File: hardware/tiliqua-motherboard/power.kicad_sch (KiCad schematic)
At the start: 23 parts, among them J6 CONN 2x5 P=2.54mm, U5 AP63200WU

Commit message: R2 start
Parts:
- removed C35: 100nF, Capacitor_SMD:C_0603_1608Metric, symbol Device:C_Small
- removed C36: 22.0uF, Capacitor_Tantalum_SMD:CP_EIA-3216-10_Kemet-I, symbol Device:C_Polarized_Small
- removed D6: 1N4007FL, Diode_SMD:D_SOD-123F, symbol Diode:US1G
- added C27, C29, C39: 47uF, Capacitor_SMD:CP_Elec_6.3x5.4, symbol Device:C_Polarized_Small
- added C28: 100nF, Capacitor_SMD:C_0603_1608Metric, symbol Device:C_Small
- added C38: 22uF, Capacitor_Tantalum_SMD:CP_EIA-3216-10_Kemet-I, symbol Device:C_Polarized_Small
- added L4, L5, L6, L7: FERRITE, Inductor_SMD:L_0603_1608Metric, symbol Device:L_Ferrite_Small
- added U6: AMS1117-3.3, Package_TO_SOT_SMD:SOT-223-3_TabPin2, symbol Regulator_Linear:AMS1117-3.3
- C32: value 22.0uF -> 22uF
- C33: value 22.0uF -> 47uF; footprint Capacitor_Tantalum_SMD:CP_EIA-3216-10_Kemet-I -> Capacitor_SMD:CP_Elec_6.3x5.4; lcsc# C782264 -> C88735; mfg# CA45-A-16V-22uF-K -> 25SEV47M6.3X5.5
- L3: value 6.8uH 2A -> 10uH 2A; lcsc# C844992 -> (none)
- R17: value 182K -> 157K; PN RC0402FR-074K7L -> (none); lcsc# C327365 -> (none)
- R18: value 62K -> 30K; PN RC0402FR-074K7L -> (none); lcsc# C137950 -> (none)
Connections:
- net VAUX is gone; now on net +12V: U5.2 (EN), U5.3 (IN)
- net +12V: now also C27.1, L6.2
- net +3V3: now also U6.2 (VO); no longer C31.2, C34.1, L3.2, R17.2
- net -12V: now also L7.2
- net GND: now also C27.2, C28.2, C29.2, C38.2, C39.2, U6.1 (GND)
- net at D3.2 (A), L2.2: now also L7.1
- net at D2.1 (K), L1.2: now also L6.1
- new net: C28.1, C29.1, L4.1, L5.1, U6.3 (VI)
- new net +5V: C31.2, C34.1, C38.1, C39.1, L3.2, L4.2, L5.2, R17.2
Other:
- moved on the sheet: C22, C23, C24, C25, C34

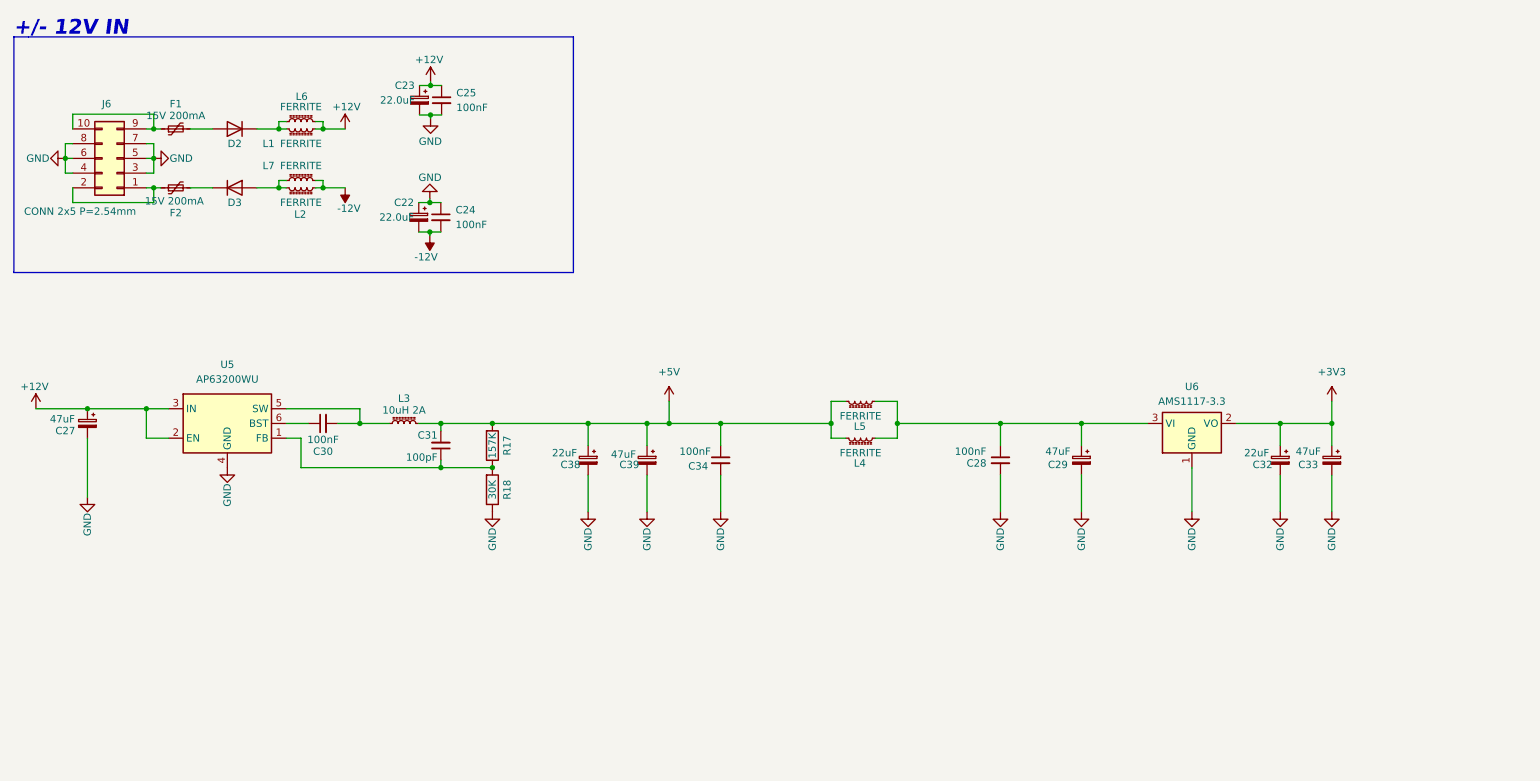
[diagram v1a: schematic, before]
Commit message: schematic cleanup, dual-role usb c
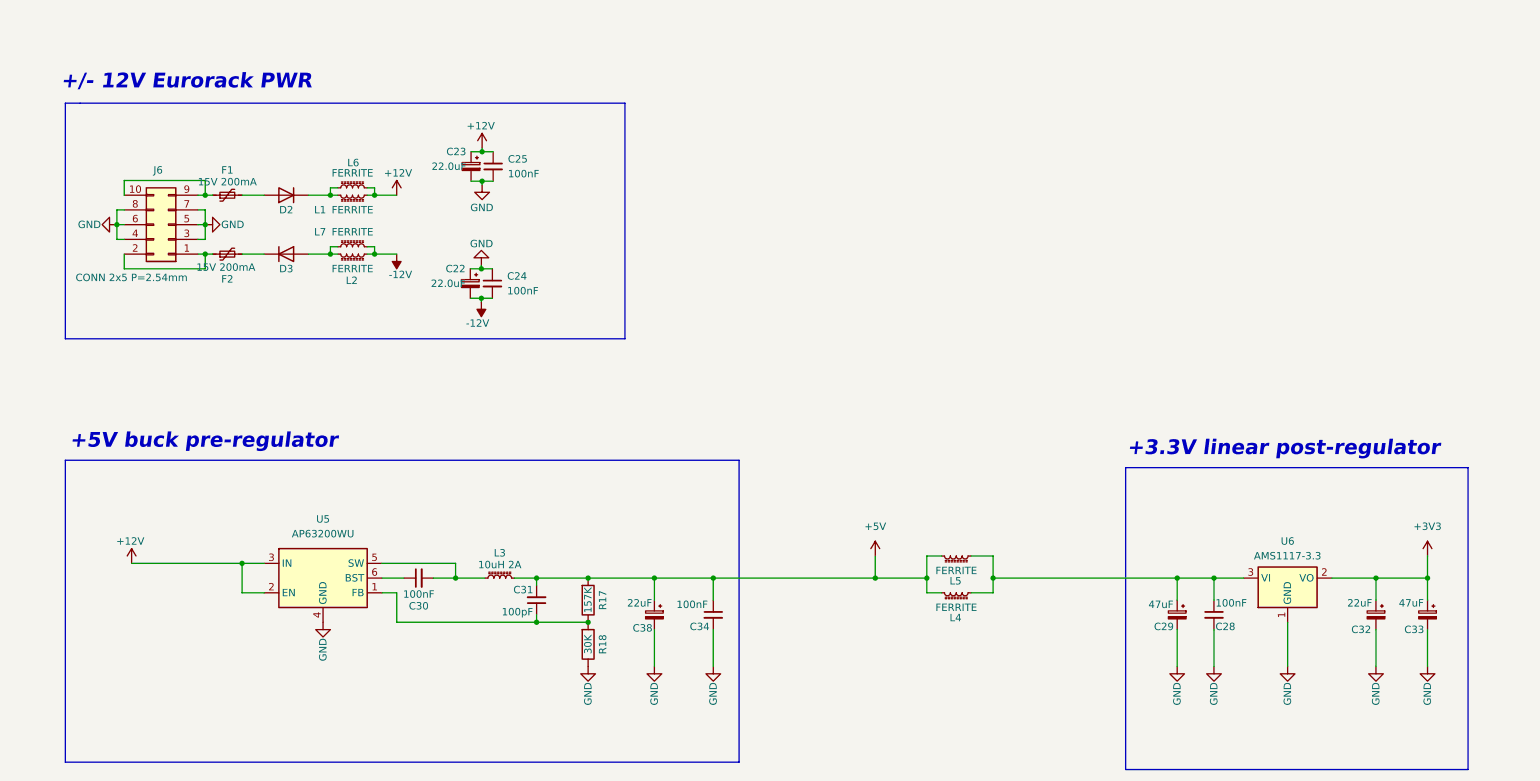
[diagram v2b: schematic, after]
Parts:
- removed C27, C39: 47uF, Capacitor_SMD:CP_Elec_6.3x5.4, symbol Device:C_Polarized_Small
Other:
- note added: "+/- 12V Eurorack PWR"
- note added: "+3.3V linear post-regulator"
- note added: "+5V buck pre-regulator"
- note removed: "+/- 12V IN"
- moved on the sheet: C22, C23, C24, C25, C28, C29, C30, C31, C32, C33, C34, C38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

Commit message: place most parts
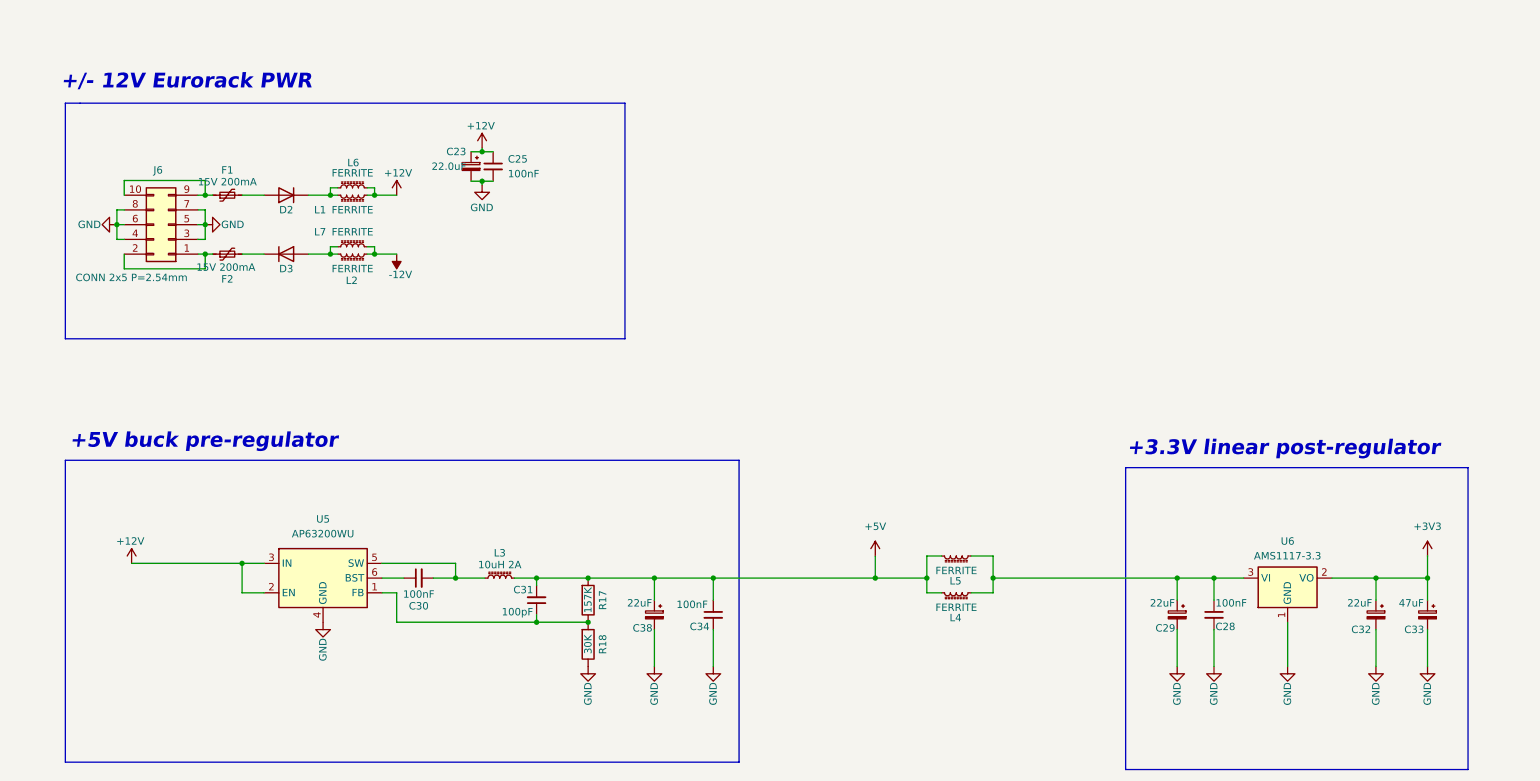
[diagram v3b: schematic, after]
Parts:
- removed C22: 22.0uF, Capacitor_Tantalum_SMD:CP_EIA-3216-10_Kemet-I, symbol Device:C_Polarized_Small
- removed C24: 100nF, Capacitor_SMD:C_0603_1608Metric, symbol Device:C_Small
- C29: value 47uF -> 22uF; footprint Capacitor_SMD:CP_Elec_6.3x5.4 -> Capacitor_Tantalum_SMD:CP_EIA-3216-10_Kemet-I; lcsc# C88735 -> C782264; mfg# 25SEV47M6.3X5.5 -> CA45-A-16V-22uF-K

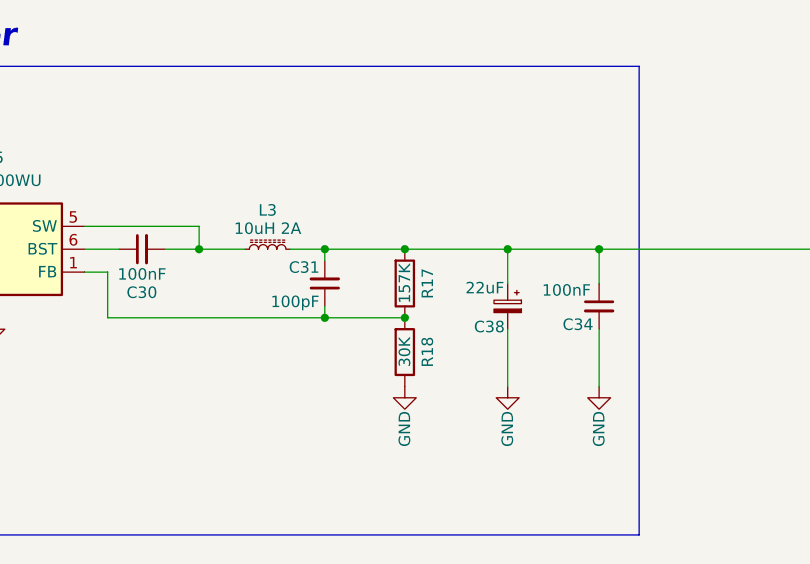
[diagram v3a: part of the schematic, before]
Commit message: add some part numbers
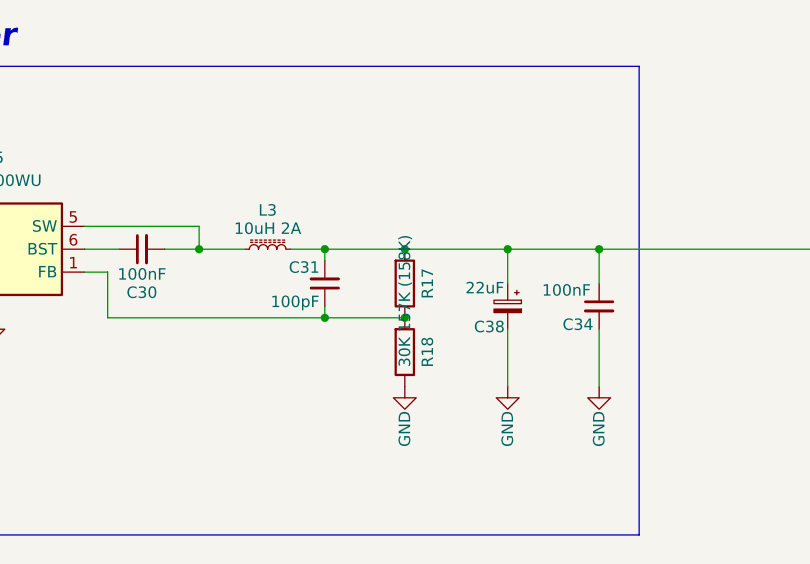
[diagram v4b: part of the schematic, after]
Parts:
- L3: lcsc# (none) -> C844996
- R17: value 157K -> 157K (158K); lcsc# (none) -> C861679
- R18: lcsc# (none) -> C25776
- U6: lcsc# (none) -> C347222

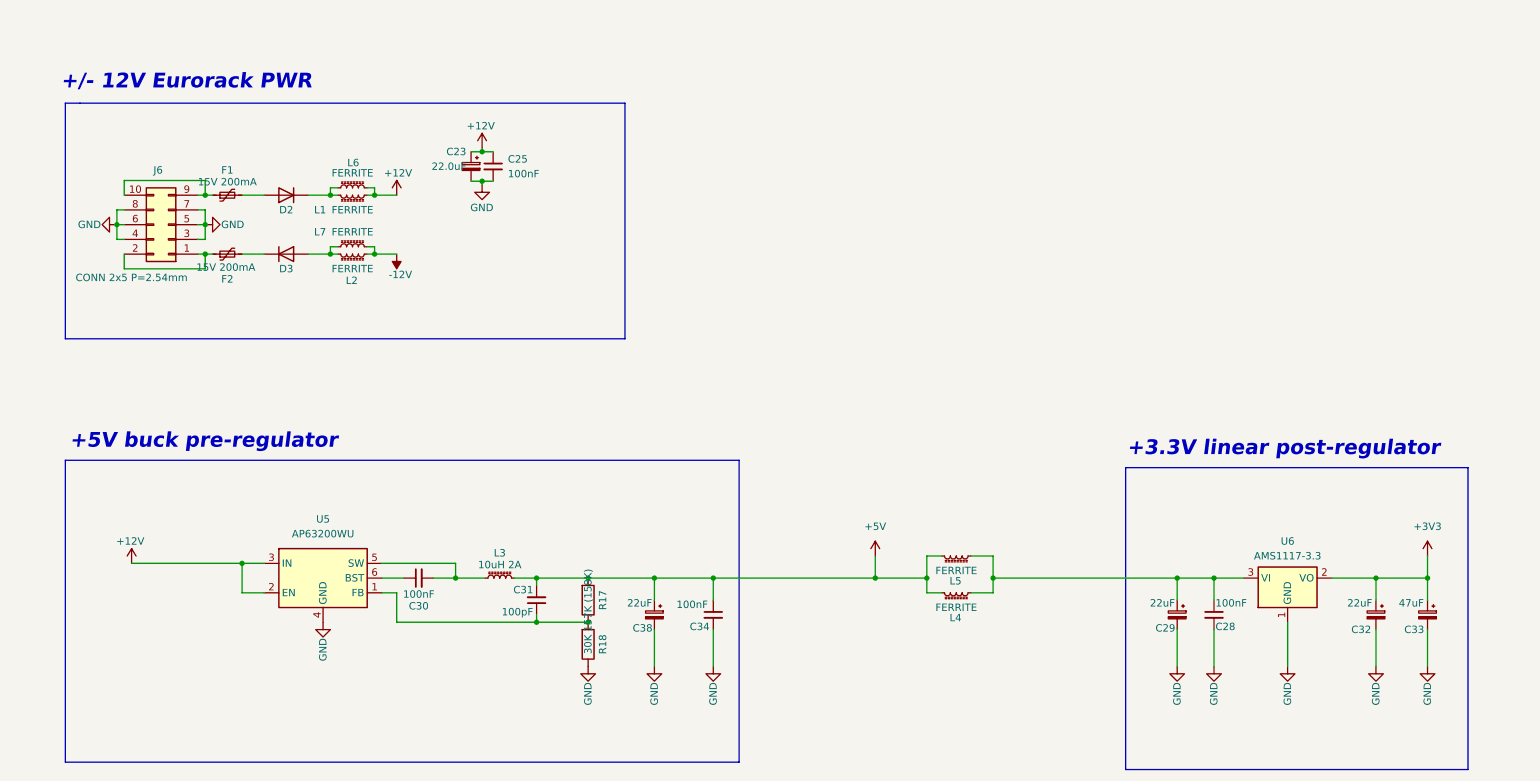
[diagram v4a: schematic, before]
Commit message: hw/mobo-r3: swap tantalums for ceramics, clean up PSU routing, swap LDO for TPS7A91, add choke input capacitors
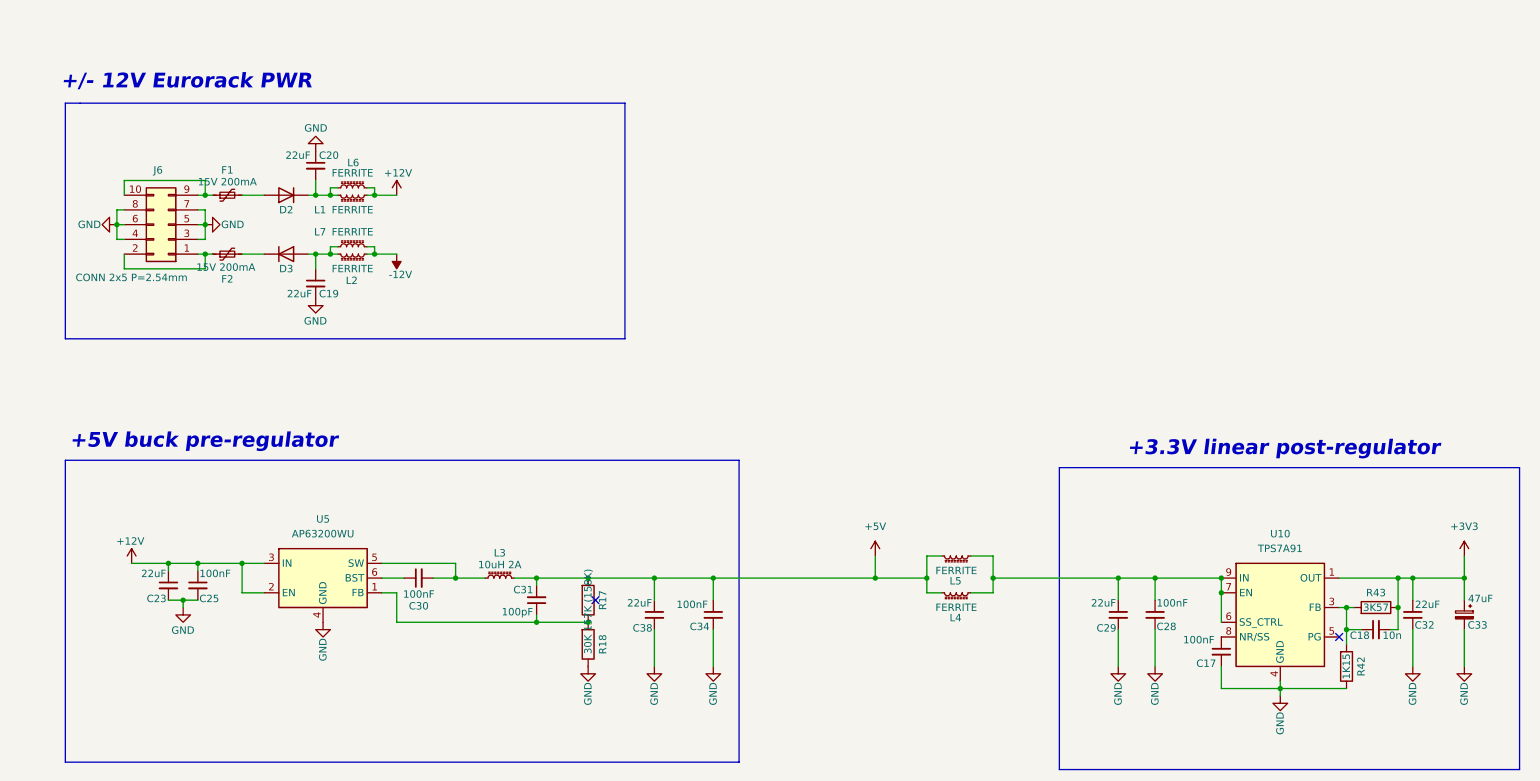
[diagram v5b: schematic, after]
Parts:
- removed C23: 22.0uF, Capacitor_Tantalum_SMD:CP_EIA-3216-10_Kemet-I, symbol Device:C_Polarized_Small
- removed C29, C32: 22uF, Capacitor_Tantalum_SMD:CP_EIA-3216-10_Kemet-I, symbol Device:C_Polarized_Small
- removed U6: AMS1117-3.3, Package_TO_SOT_SMD:SOT-223-3_TabPin2, symbol Regulator_Linear:AMS1117-3.3
- added C17: 100nF, Capacitor_SMD:C_0402_1005Metric, symbol Device:C_Small
- added C18: 10n, Capacitor_SMD:C_0402_1005Metric, symbol Device:C_Small
- added C19, C20, C23, C29, C32: 22uF, Capacitor_SMD:C_1206_3216Metric, symbol Device:C_Small
- added R42: 1K15, Resistor_SMD:R_0402_1005Metric, symbol Device:R
- added R43: 3K57, Resistor_SMD:R_0402_1005Metric, symbol Device:R
- added U10: TPS7A91, Package_DFN_QFN:Texas_S-PDSO-N10_EP1.2x2mm_ThermalVias, symbol Regulator_Linear:TPS7A91
- C25, C28, C30: footprint Capacitor_SMD:C_0603_1608Metric -> Capacitor_SMD:C_0402_1005Metric; lcsc# C14663 -> (none); mfg# C1608X7R1E104KT000N -> (none)
- C31: footprint Capacitor_SMD:C_0603_1608Metric -> Capacitor_SMD:C_0402_1005Metric; lcsc# C14858 -> (none); mfg# C1608X7R1E104KT000N -> (none)
- C38: footprint Capacitor_Tantalum_SMD:CP_EIA-3216-10_Kemet-I -> Capacitor_SMD:C_1206_3216Metric; symbol Device:C_Polarized_Small -> Device:C_Small; lcsc# C782264 -> C12891; mfg# CA45-A-16V-22uF-K -> CL31A226KAHNNNE
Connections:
- net +12V: now also C23.1
- net +3V3: now also C18.2, C32.1, R43.1, U10.1 (OUT), U10.2 (OUT)
- net GND: now also C17.2, C19.2, C20.1, C23.2, C29.2, C32.2, R42.1, U10.11 (GND), U10.4 (GND)
- net at D3.2 (A), L2.2, L7.1: now also C19.1
- net at C28.1, L4.1, L5.1: now also C29.1, U10.10 (IN), U10.6 (SS_CTRL), U10.7 (EN), U10.9 (IN)
- net at D2.1 (K), L1.2, L6.1: now also C20.2
- new net: C17.1, U10.8 (NR/SS)
- new net: C18.1, R42.2, R43.2, U10.3 (FB)
- no-connect marks 0 -> 2
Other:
- moved on the sheet: C25, C28, C33

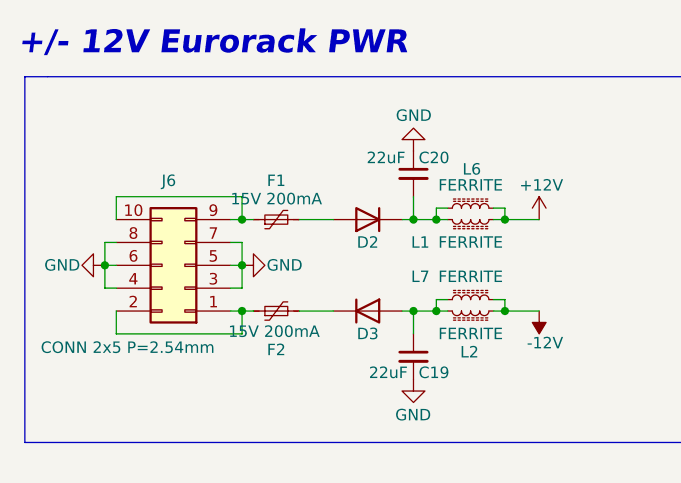
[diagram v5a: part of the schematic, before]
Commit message: hw/mobo-r3: +5V I2C bridge fix + EN, +12V ingress 200mA->350mA fuse, GPDI +5V NONE->50mA fuse
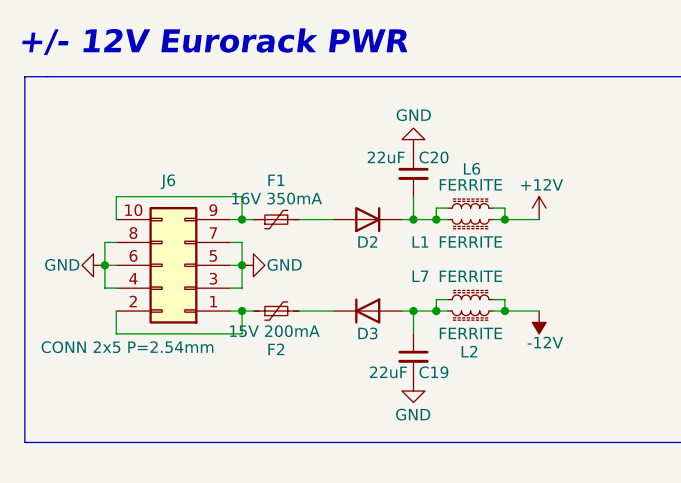
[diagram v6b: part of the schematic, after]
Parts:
- F1: value 15V 200mA -> 16V 350mA; lcsc# C883103 -> C883107
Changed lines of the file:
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@@
 			)
 		)
-		(property "Value" "15V 200mA"
+		(property "Value" "16V 350mA"
 			(at 55.88 45.974 90)
 			(effects
@@
 			)
 		)
-		(property "lcsc#" "C883103"
+		(property "lcsc#" "C883107"
 			(at 55.88 48.26 90)
 			(effects
